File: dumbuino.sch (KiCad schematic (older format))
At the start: 8 parts, among them P1 Power, P2 Analog, P3 Digital, P4 Digital, P5 CONN_01X01, P6 CONN_01X01, P7 CONN_01X01, P8 CONN_01X01

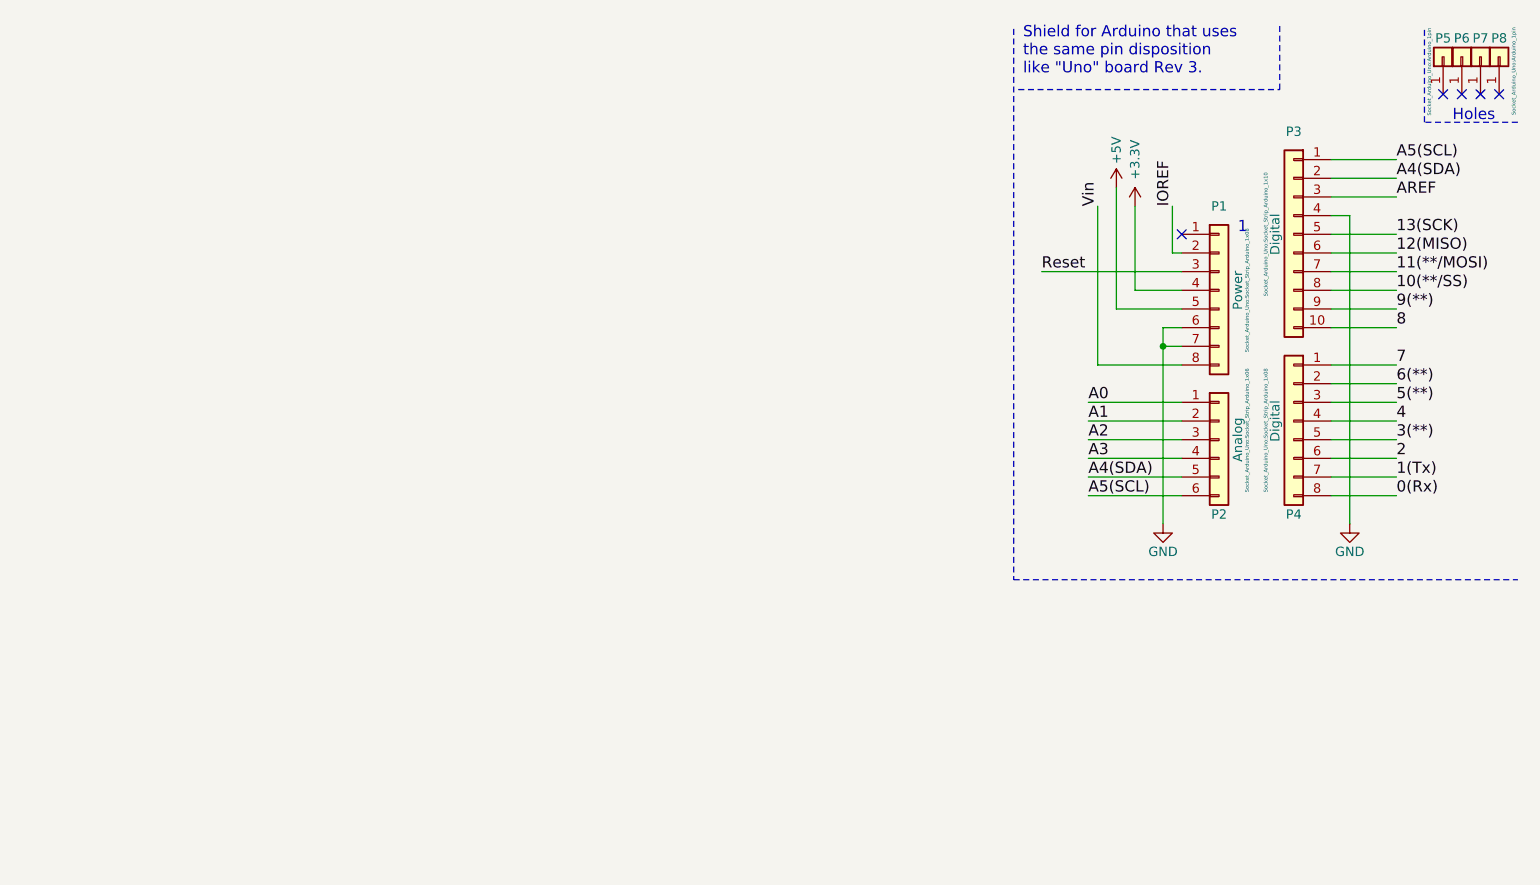
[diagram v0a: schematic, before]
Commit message: Added arduino schematic
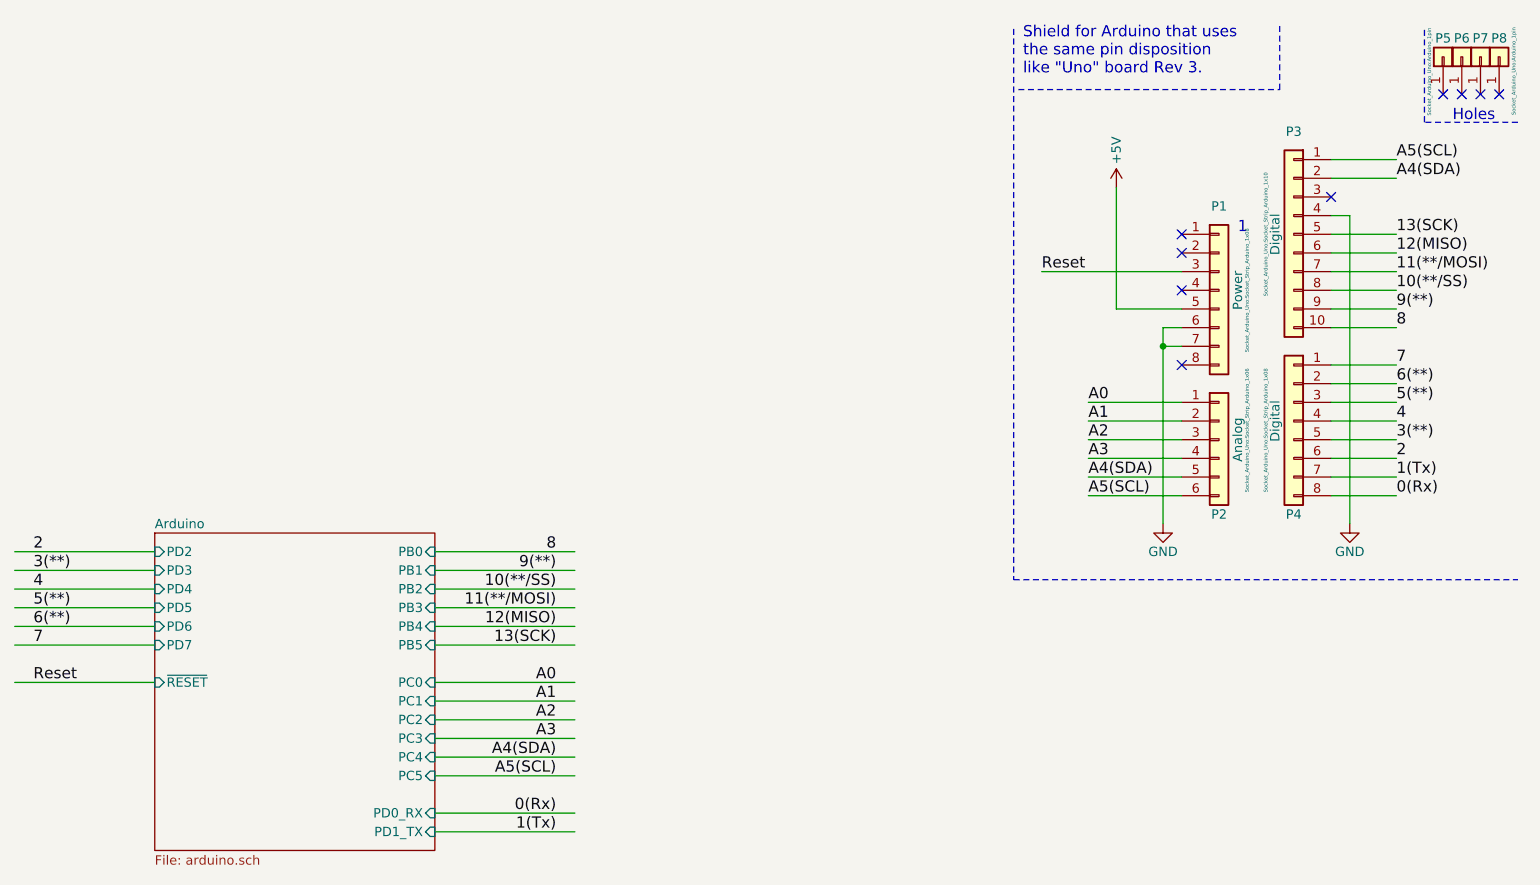
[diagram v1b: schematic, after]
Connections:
- net labels removed: +3.3V, AREF, IOREF, Vin
- wire segments 38 -> 52
- no-connect marks 5 -> 9
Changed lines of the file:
@@
 EESchema Schematic File Version 4
-LIBS:Arduino_As_Uno-cache
-EELAYER 26 0
+EELAYER 30 0
 EELAYER END
 $Descr A4 11693 8268
 encoding utf-8
-Sheet 1 1
-Title ""
-Date "lun. 30 mars 2015"
-Rev ""
+Sheet 1 2
+Title "Dumbuino"
+Date "2020-09-20"
+Rev "v01"
 Comp ""
 Comment1 ""
 Comment2 ""
 Comment3 ""
-Comment4 ""
+Comment4 "Author: Sebastian Sole"
 $EndDescr
-Text Label 8950 1450 1    60   ~ 0
-Vin
-Text Label 9350 1450 1    60   ~ 0
-IOREF
 Text Label 8900 2500 0    60   ~ 0
 A0
@@
 Text Label 10550 1600 0    60   ~ 0
 13(SCK)
-Text Label 10550 1400 0    60   ~ 0
-AREF
 NoConn ~ 9400 1600
 Text Label 10550 1300 0    60   ~ 0
@@
 Reset
 $Comp
-L power:+3.3V #PWR01
-U 1 1 56D70538
-P 9150 1450
-F 0 "#PWR01" H 9150 1300 50  0001 C CNN
-F 1 "+3.3V" V 9150 1700 50  0000 C CNN
-F 2 "" H 9150 1450 50  0000 C CNN
-F 3 "" H 9150 1450 50  0000 C CNN
-	1    9150 1450
-	1    0    0    -1
-$EndComp
-$Comp
 L power:+5V #PWR02
 U 1 1 56D707BB
@@
 	9925 825  9925 475
 Wire Wire Line
-	9350 1450 9350 1700
-Wire Wire Line
-	9350 1700 9400 1700
-Wire Wire Line
-	9400 1900 9150 1900
-Wire Wire Line
 	9400 2000 9050 2000
-Wire Wire Line
-	9400 2300 8950 2300
 Wire Wire Line
 	9400 2100 9300 2100
@@
 Connection ~ 9300 2200
 Wire Wire Line
-	8950 2300 8950 1450
-Wire Wire Line
 	9050 2000 9050 1350
-Wire Wire Line
-	9150 1900 9150 1450
 Wire Wire Line
 	9400 2500 8900 2500
@@
 	10200 1600 10550 1600
 Wire Wire Line
-	10200 1400 10550 1400
-Wire Wire Line
 	10200 1300 10550 1300
 Wire Wire Line
@@
 Wire Notes Line
 	10700 1000 10700 500
+$Sheet
+S 3900 3200 1500 1700
+U 5F673CBC
+F0 "Arduino" 50
+F1 "arduino.sch" 50
+F2 "PC0" I R 5400 4000 50
+F3 "PC1" I R 5400 4100 50
+F4 "PC2" I R 5400 4200 50
+F5 "PC3" I R 5400 4300 50
+F6 "PC5" I R 5400 4500 50
+F7 "PC4" I R 5400 4400 50
+F8 "PB0" I R 5400 3300 50
+F9 "PB1" I R 5400 3400 50
+F10 "PB2" I R 5400 3500 50
+F11 "PB3" I R 5400 3600 50
+F12 "PB5" I R 5400 3800 50
+F13 "PB4" I R 5400 3700 50
+F14 "PD0_RX" I R 5400 4700 50
+F15 "PD1_TX" I R 5400 4800 50
+F16 "PD2" I L 3900 3300 50
+F17 "PD3" I L 3900 3400 50
+F18 "PD4" I L 3900 3500 50
+F19 "PD7" I L 3900 3800 50
+F20 "PD5" I L 3900 3600 50
+F21 "PD6" I L 3900 3700 50
+F22 "~RESET" I L 3900 4000 50
+$EndSheet
+NoConn ~ 9400 1900
+NoConn ~ 9400 1700
+NoConn ~ 9400 2300
+Text Label 6050 4100 2    60   ~ 0
+A1
+Text Label 6050 4200 2    60   ~ 0
+A2
+Text Label 6050 4300 2    60   ~ 0
+A3
+Text Label 6050 4400 2    60   ~ 0
+A4(SDA)
+Text Label 6050 4500 2    60   ~ 0
+A5(SCL)
+Wire Wire Line
+	5400 4100 6150 4100
+Wire Wire Line
+	5400 4200 6150 4200
+Wire Wire Line
+	5400 4300 6150 4300
+Wire Wire Line
+	5400 4400 6150 4400
+Wire Wire Line
+	5400 4500 6150 4500
+Wire Wire Line
+	5400 4000 6150 4000
+Text Label 6050 4000 2    60   ~ 0
+A0
+NoConn ~ 10200 1400
+Wire Wire Line
+	5400 3300 6150 3300
+Wire Wire Line
+	5400 3400 6150 3400
+Wire Wire Line
+	5400 3500 6150 3500
+Wire Wire Line
+	5400 3600 6150 3600
+Wire Wire Line
+	5400 3700 6150 3700
+Wire Wire Line
+	5400 3800 6150 3800
+Wire Wire Line
+	5400 4800 6150 4800
+Wire Wire Line
+	5400 4700 6150 4700
+Text Label 6050 3800 2    60   ~ 0
+13(SCK)
+Text Label 6050 3700 2    60   ~ 0
+12(MISO)
+Text Label 6050 3600 2    60   ~ 0
+11(**/MOSI)
+Text Label 6050 3500 2    60   ~ 0
+10(**/SS)
+Text Label 6050 3400 2    60   ~ 0
+9(**)
+Text Label 6050 3300 2    60   ~ 0
+8
+Text Label 6050 4800 2    60   ~ 0
+1(Tx)
+Text Label 6050 4700 2    60   ~ 0
+0(Rx)
+Wire Wire Line
+	3900 3800 3150 3800
+Wire Wire Line
+	3900 3700 3150 3700
+Wire Wire Line
+	3900 3600 3150 3600
+Wire Wire Line
+	3900 3500 3150 3500
+Wire Wire Line
+	3900 3400 3150 3400
+Wire Wire Line
+	3900 3300 3150 3300
+Text Label 3250 3800 0    60   ~ 0
+7
+Text Label 3250 3700 0    60   ~ 0
+6(**)
+Text Label 3250 3600 0    60   ~ 0
+5(**)
+Text Label 3250 3300 0    60   ~ 0
+2
+Text Label 3250 3400 0    60   ~ 0
+3(**)
+Text Label 3250 3500 0    60   ~ 0
+4
+Wire Wire Line
+	3900 4000 3150 4000
+Text Label 3250 4000 0    60   ~ 0
+Reset
 $EndSCHEMATC

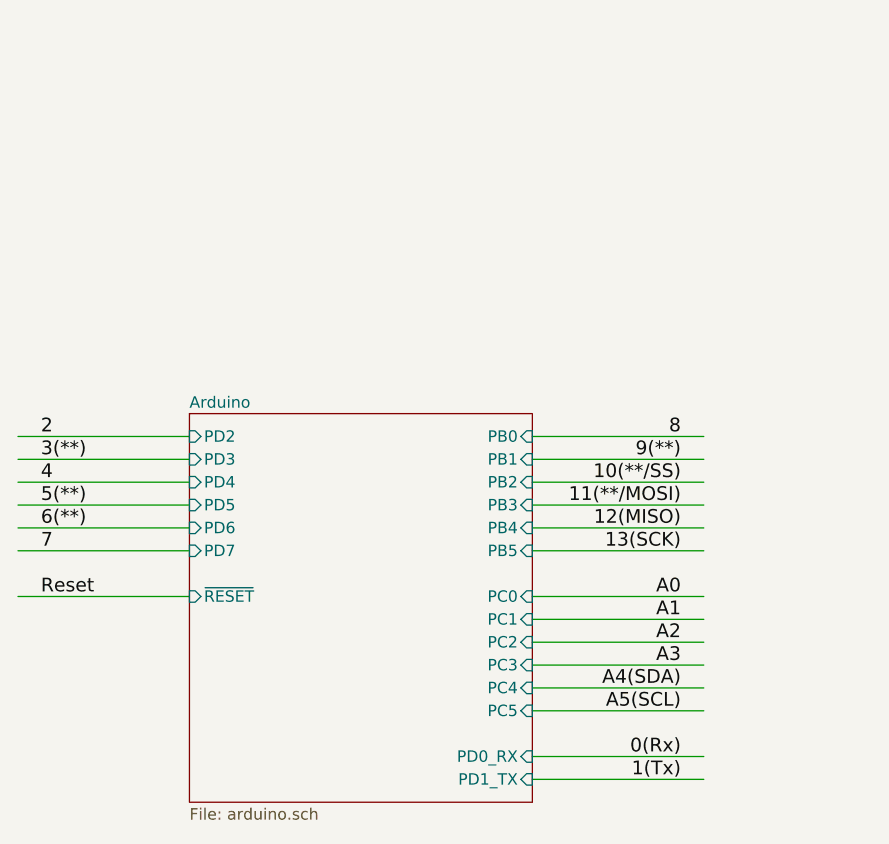
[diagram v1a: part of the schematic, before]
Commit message: Added two 48V digital outputs
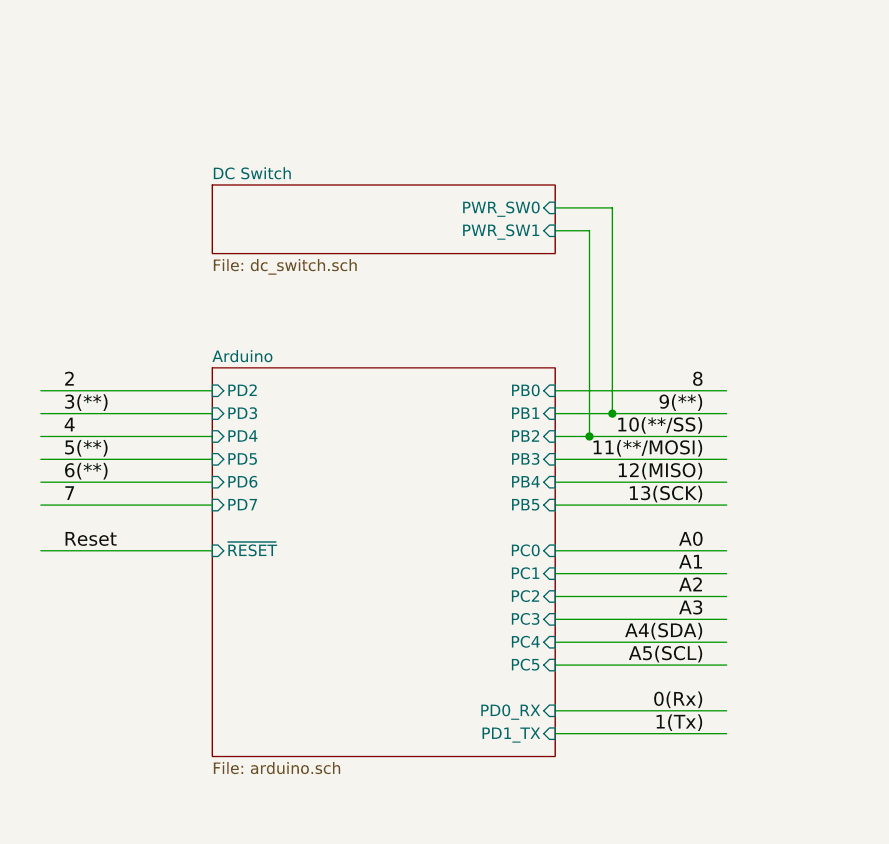
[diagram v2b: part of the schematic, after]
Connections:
- wire segments 52 -> 58
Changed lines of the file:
@@
 $Descr A4 11693 8268
 encoding utf-8
-Sheet 1 2
+Sheet 1 3
 Title "Dumbuino"
 Date "2020-09-20"
@@
 	10700 1000 10700 500
 $Sheet
-S 3900 3200 1500 1700
+S 4000 3000 1500 1700
 U 5F673CBC
 F0 "Arduino" 50
 F1 "arduino.sch" 50
-F2 "PC0" I R 5400 4000 50
-F3 "PC1" I R 5400 4100 50
-F4 "PC2" I R 5400 4200 50
-F5 "PC3" I R 5400 4300 50
-F6 "PC5" I R 5400 4500 50
-F7 "PC4" I R 5400 4400 50
-F8 "PB0" I R 5400 3300 50
-F9 "PB1" I R 5400 3400 50
-F10 "PB2" I R 5400 3500 50
-F11 "PB3" I R 5400 3600 50
-F12 "PB5" I R 5400 3800 50
-F13 "PB4" I R 5400 3700 50
-F14 "PD0_RX" I R 5400 4700 50
-F15 "PD1_TX" I R 5400 4800 50
-F16 "PD2" I L 3900 3300 50
-F17 "PD3" I L 3900 3400 50
-F18 "PD4" I L 3900 3500 50
-F19 "PD7" I L 3900 3800 50
-F20 "PD5" I L 3900 3600 50
-F21 "PD6" I L 3900 3700 50
-F22 "~RESET" I L 3900 4000 50
+F2 "PC0" I R 5500 3800 50
+F3 "PC1" I R 5500 3900 50
+F4 "PC2" I R 5500 4000 50
+F5 "PC3" I R 5500 4100 50
+F6 "PC5" I R 5500 4300 50
+F7 "PC4" I R 5500 4200 50
+F8 "PB0" I R 5500 3100 50
+F9 "PB1" I R 5500 3200 50
+F10 "PB2" I R 5500 3300 50
+F11 "PB3" I R 5500 3400 50
+F12 "PB5" I R 5500 3600 50
+F13 "PB4" I R 5500 3500 50
+F14 "PD0_RX" I R 5500 4500 50
+F15 "PD1_TX" I R 5500 4600 50
+F16 "PD2" I L 4000 3100 50
+F17 "PD3" I L 4000 3200 50
+F18 "PD4" I L 4000 3300 50
+F19 "PD7" I L 4000 3600 50
+F20 "PD5" I L 4000 3400 50
+F21 "PD6" I L 4000 3500 50
+F22 "~RESET" I L 4000 3800 50
 $EndSheet
 NoConn ~ 9400 1900
 NoConn ~ 9400 1700
 NoConn ~ 9400 2300
-Text Label 6050 4100 2    60   ~ 0
+Text Label 6150 3900 2    60   ~ 0
 A1
-Text Label 6050 4200 2    60   ~ 0
+Text Label 6150 4000 2    60   ~ 0
 A2
-Text Label 6050 4300 2    60   ~ 0
+Text Label 6150 4100 2    60   ~ 0
 A3
-Text Label 6050 4400 2    60   ~ 0
+Text Label 6150 4200 2    60   ~ 0
 A4(SDA)
-Text Label 6050 4500 2    60   ~ 0
+Text Label 6150 4300 2    60   ~ 0
 A5(SCL)
 Wire Wire Line
-	5400 4100 6150 4100
-Wire Wire Line
-	5400 4200 6150 4200
-Wire Wire Line
-	5400 4300 6150 4300
-Wire Wire Line
-	5400 4400 6150 4400
-Wire Wire Line
-	5400 4500 6150 4500
-Wire Wire Line
-	5400 4000 6150 4000
-Text Label 6050 4000 2    60   ~ 0
+	5500 3900 6250 3900
+Wire Wire Line
+	5500 4000 6250 4000
+Wire Wire Line
+	5500 4100 6250 4100
+Wire Wire Line
+	5500 4200 6250 4200
+Wire Wire Line
+	5500 4300 6250 4300
+Wire Wire Line
+	5500 3800 6250 3800
+Text Label 6150 3800 2    60   ~ 0
 A0
 NoConn ~ 10200 1400
 Wire Wire Line
-	5400 3300 6150 3300
-Wire Wire Line
-	5400 3400 6150 3400
-Wire Wire Line
-	5400 3500 6150 3500
-Wire Wire Line
-	5400 3600 6150 3600
-Wire Wire Line
-	5400 3700 6150 3700
-Wire Wire Line
-	5400 3800 6150 3800
-Wire Wire Line
-	5400 4800 6150 4800
-Wire Wire Line
-	5400 4700 6150 4700
-Text Label 6050 3800 2    60   ~ 0
+	5500 3300 5650 3300
+Wire Wire Line
+	5500 3400 6250 3400
+Wire Wire Line
+	5500 3500 6250 3500
+Wire Wire Line
+	5500 3600 6250 3600
+Wire Wire Line
+	5500 4600 6250 4600
+Wire Wire Line
+	5500 4500 6250 4500
+Text Label 6150 3600 2    60   ~ 0
 13(SCK)
-Text Label 6050 3700 2    60   ~ 0
+Text Label 6150 3500 2    60   ~ 0
 12(MISO)
-Text Label 6050 3600 2    60   ~ 0
+Text Label 6150 3400 2    60   ~ 0
 11(**/MOSI)
-Text Label 6050 3500 2    60   ~ 0
+Text Label 6150 3300 2    60   ~ 0
 10(**/SS)
-Text Label 6050 3400 2    60   ~ 0
+Text Label 6150 3200 2    60   ~ 0
 9(**)
-Text Label 6050 3300 2    60   ~ 0
+Text Label 6150 3100 2    60   ~ 0
 8
-Text Label 6050 4800 2    60   ~ 0
+Text Label 6150 4600 2    60   ~ 0
 1(Tx)
-Text Label 6050 4700 2    60   ~ 0
+Text Label 6150 4500 2    60   ~ 0
 0(Rx)
 Wire Wire Line
-	3900 3800 3150 3800
-Wire Wire Line
-	3900 3700 3150 3700
-Wire Wire Line
-	3900 3600 3150 3600
-Wire Wire Line
-	3900 3500 3150 3500
-Wire Wire Line
-	3900 3400 3150 3400
-Wire Wire Line
-	3900 3300 3150 3300
-Text Label 3250 3800 0    60   ~ 0
+	4000 3600 3250 3600
+Wire Wire Line
+	4000 3500 3250 3500
+Wire Wire Line
+	4000 3400 3250 3400
+Wire Wire Line
+	4000 3300 3250 3300
+Wire Wire Line
+	4000 3200 3250 3200
+Wire Wire Line
+	4000 3100 3250 3100
+Text Label 3350 3600 0    60   ~ 0
 7
-Text Label 3250 3700 0    60   ~ 0
+Text Label 3350 3500 0    60   ~ 0
 6(**)
-Text Label 3250 3600 0    60   ~ 0
+Text Label 3350 3400 0    60   ~ 0
 5(**)
-Text Label 3250 3300 0    60   ~ 0
+Text Label 3350 3100 0    60   ~ 0
 2
-Text Label 3250 3400 0    60   ~ 0
+Text Label 3350 3200 0    60   ~ 0
 3(**)
-Text Label 3250 3500 0    60   ~ 0
+Text Label 3350 3300 0    60   ~ 0
 4
 Wire Wire Line
-	3900 4000 3150 4000
-Text Label 3250 4000 0    60   ~ 0
+	4000 3800 3250 3800
+Text Label 3350 3800 0    60   ~ 0
 Reset
+$Sheet
+S 4000 2200 1500 300
+U 5FEEE9CE
+F0 "DC Switch" 50
+F1 "dc_switch.sch" 50
+F2 "PWR_SW0" I R 5500 2300 50
+F3 "PWR_SW1" I R 5500 2400 50
+$EndSheet
+Wire Wire Line
+	5500 2300 5750 2300
+Wire Wire Line
+	5500 2400 5650 2400
+Wire Wire Line
+	5500 3200 5750 3200
+Wire Wire Line
+	5500 3100 6250 3100
+Wire Wire Line
+	5750 2300 5750 3200
+Connection ~ 5750 3200
+Wire Wire Line
+	5750 3200 6250 3200
+Wire Wire Line
+	5650 2400 5650 3300
+Connection ~ 5650 3300
+Wire Wire Line
+	5650 3300 6250 3300
 $EndSCHEMATC
